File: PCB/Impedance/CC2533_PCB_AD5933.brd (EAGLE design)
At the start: 69.5 x 40.3 mm, 34 parts

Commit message: New updates
Added new layout of CC2533 voltage stim and AD5933 impeance analysis
with ground planes (completed), and that of AD5933 impedance analysis
only.
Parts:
- removed U$13, U$15: SPDT_DUAL, CC2530_PCB_TL:SPDT_DUAL
- moved U$16 10.1 mm to (37.6, 8.31)
- moved U$21 10.1 mm to (31.9, 9.86)
- moved U$22 10.1 mm to (31.9, 6.97)
- moved U$19 7.75 mm to (32.4, 16.0)
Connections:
- removed net IN1: U$1.P1_1, U$13.IN1, U$13.IN2, U$15.IN1, U$15.IN2
- removed net N$15: U$15.COM1, U$30.2
- removed net N$30: U$15.COM2, U$30.5
- removed net N$31: U$13.NO1, U$19.NO2
- removed net N$32: U$13.NO2, U$19.NC2
- net GND: no longer U$13.GND, U$15.GND
- net LEFT: no longer U$15.NC1
- net N$10: now also U$19.NC2; no longer U$13.COM2
- net N$7: now also U$30.2; no longer U$15.NO1
- net N$8: now also U$30.5; no longer U$15.NO2
- net N$9: now also U$19.NO2; no longer U$13.COM1
- net P0_1: no longer U$13.NC1
- net P0_3: no longer U$13.NC2
- net RIGHT: no longer U$15.NC2
- net VDD: no longer U$13.V+, U$15.V+
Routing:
- net VDD: track 119.2 -> 38.0 mm, vias 5 -> 3
- net N$31: track 47.2 -> 0.00 mm, vias 2 -> 0
- net N$9: track 36.4 -> 0.00 mm, vias 2 -> 0
- net IN1: track 33.9 -> 0.00 mm
- net N$10: track 30.1 -> 0.00 mm, vias 2 -> 0
- net N$32: track 27.5 -> 0.00 mm, vias 2 -> 0
- net N$30: track 20.7 -> 0.00 mm, vias 2 -> 0
- net N$8: track 16.9 -> 0.00 mm, vias 2 -> 0
- net LEFT: track 16.4 -> 0.01 mm
- net N$7: track 15.0 -> 0.00 mm, vias 2 -> 0
- net N$15: track 14.8 -> 0.00 mm, vias 2 -> 0
- net N$14: track 3.72 -> 18.0 mm
- net N$13: track 3.87 -> 17.9 mm
- net IN2: track 23.5 -> 11.5 mm
- net GND: track 94.2 -> 83.4 mm
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- added copper zone on layer 1, net GND
- added copper zone on layer 16, net GND

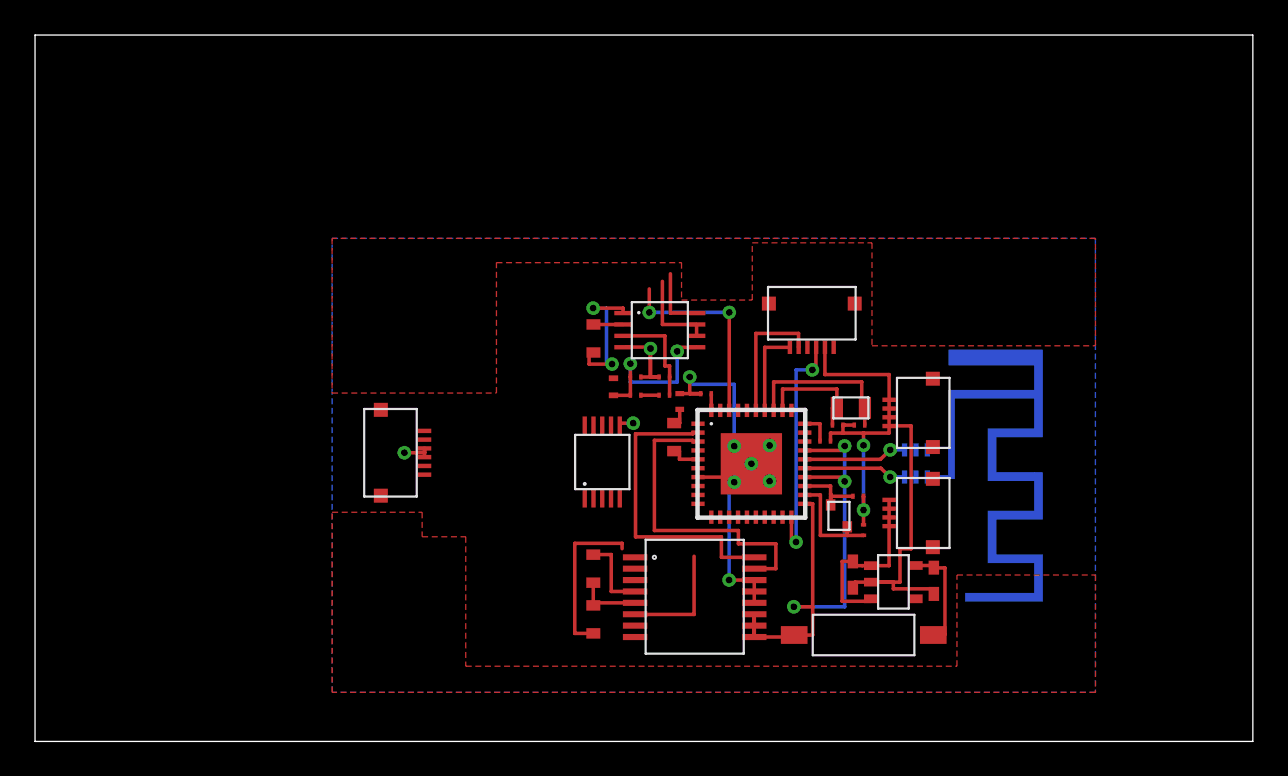
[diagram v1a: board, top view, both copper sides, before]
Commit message: Complete layouts for CC2533 circuits with AD5933
CC2533_PCB_Main_Plane - Voltage stim + Impedance Analysis.
CC2533_PCB_Biphasic - Current stim + Impedance Analysis.
CC2533_PCB_AD5933 - Impedance Analysis only.
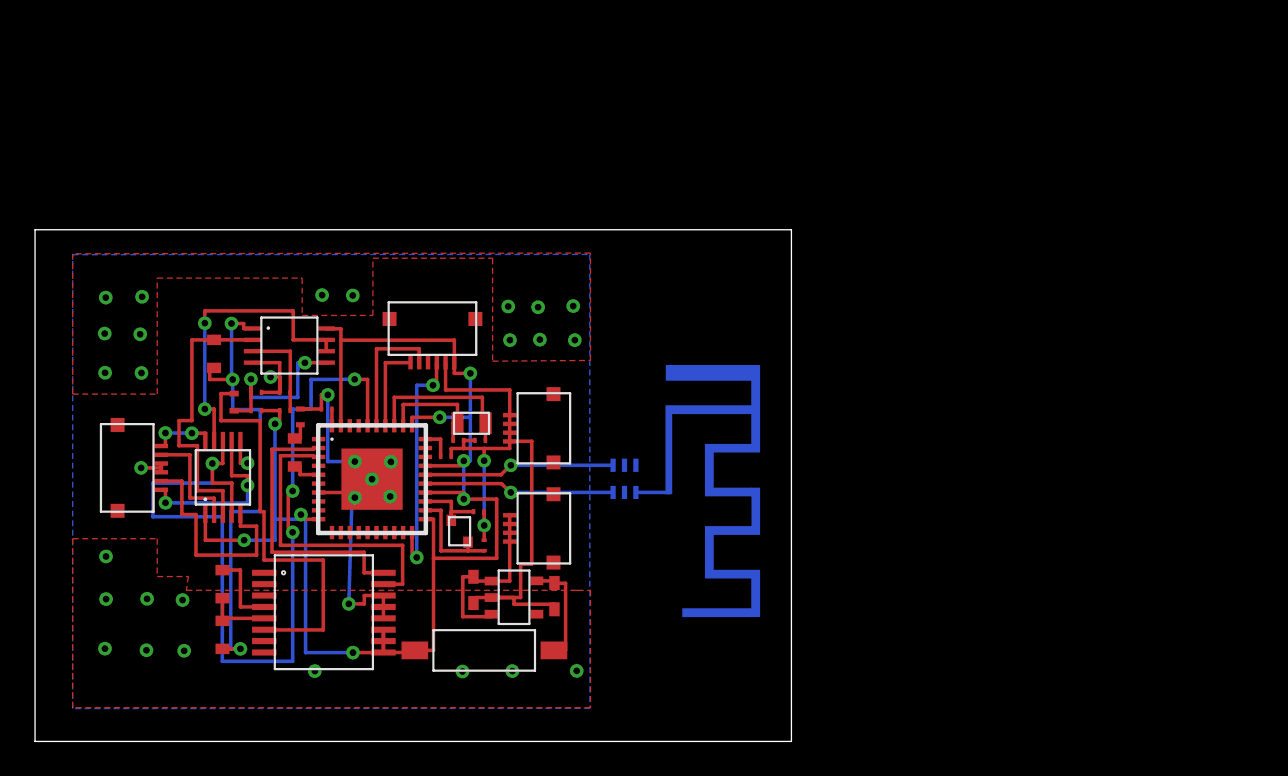
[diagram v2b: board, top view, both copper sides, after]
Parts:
- moved U$10 21.7 mm to (27.3, 8.21)
- moved U$12 21.7 mm to (25.0, 8.65)
- moved U$17 21.7 mm to (22.7, 21.6)
- moved U$19 21.7 mm to (10.7, 15.1)
- moved U$26 21.7 mm to (11.4, 19.4)
- moved U$27 21.7 mm to (12.6, 18.9)
- moved U$28 21.7 mm to (12.6, 19.9)
- moved U$29 21.7 mm to (14.8, 16.5)
- moved U$31 21.7 mm to (15.1, 18.5)
- moved U$4 21.7 mm to (25.6, 11.2)
- moved U$40 21.7 mm to (25.4, 17.2)
- moved U$5 21.7 mm to (25.3, 13.1)
- moved U$1 21.7 mm to (19.2, 15.0)
- moved U$11 21.7 mm to (29.7, 8.29)
- moved U$14 21.7 mm to (16.6, 19.0)
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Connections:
- net IN2: now also U$1.P2_0; no longer U$1.P1_6
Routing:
- net VDD: track 38.0 -> 85.0 mm, vias 3 -> 8
- net IN2: track 11.5 -> 52.4 mm, vias 2 -> 4
- net N$19: track 6.69 -> 23.4 mm
- net N$11: track 1.99 -> 16.9 mm
- net N$8: track 0.00 -> 12.9 mm
- net N$29: track 5.06 -> 17.2 mm, vias 0 -> 2
- net N$10: track 0.00 -> 10.1 mm, vias 0 -> 2
- net N$25: track 17.9 -> 27.4 mm, vias 2 -> 3
- net N$7: track 0.00 -> 6.36 mm
- net N$1: track 5.93 -> 10.9 mm
- net N$2: track 5.93 -> 10.9 mm
- net N$9: track 0.00 -> 3.72 mm, vias 0 -> 2
- net N$13: track 17.9 -> 16.6 mm
- net N$28: track 9.59 -> 10.2 mm
- net N$27: track 6.05 -> 5.54 mm
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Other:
- board size 69.5 x 40.3 mm -> 43.2 x 29.2 mm
